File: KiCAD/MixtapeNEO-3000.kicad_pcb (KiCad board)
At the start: 2 copper layers, 99 x 64.8 mm, 62 parts, among them J1 CONN_01X04, J2 CONN_01X04, J4 Con_3-5V, J6 Sync_Jumper, SW1 SW_Push, SW2 SW_Push, SW3 SW_Push, U1 ATTINY85-20SU, U2 PAM8002

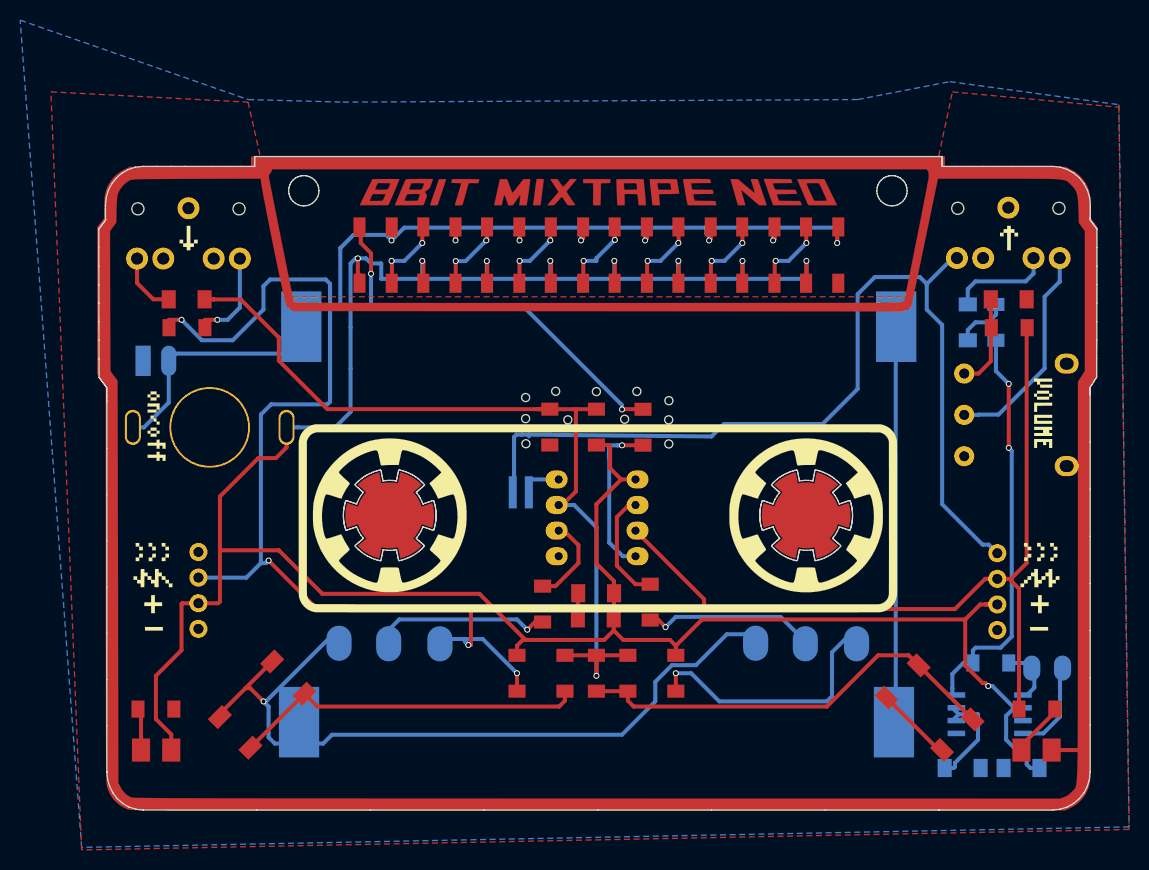
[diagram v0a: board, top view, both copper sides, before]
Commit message: reworked kicad 5 and many new design
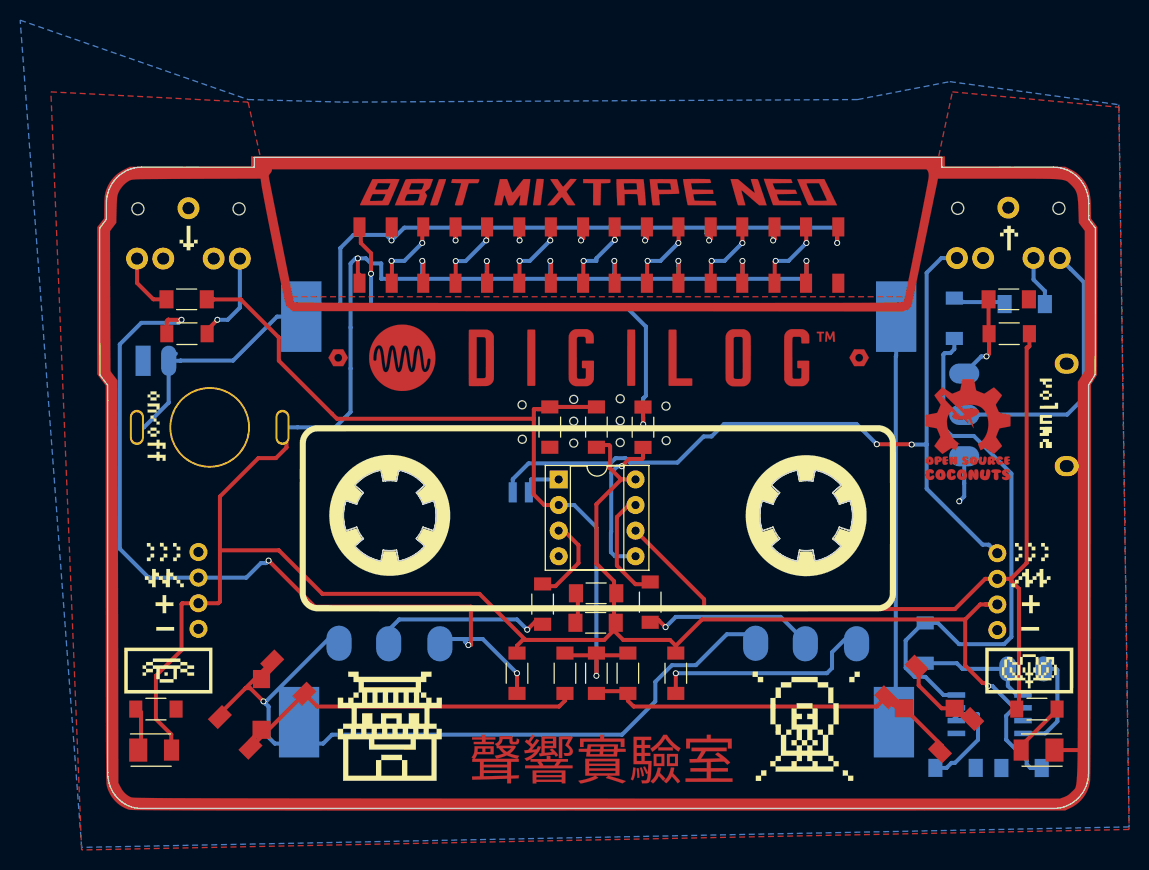
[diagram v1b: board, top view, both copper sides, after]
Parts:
- removed the ? at (142.9, 96.1)
- removed the ? at (147.0, 93.7)
- removed the ? at (142.8, 91.5)
- removed the ? at (145.8, 90.9)
- removed the ? at (149.9, 90.9)
- removed the ? at (142.8, 93.6)
- added ?: , 8BitMixtape3000-MutanMonkey:Speaker_Loch08, F.Cu at (142.5, 95.7)
- added ?: , 8BitMixtape3000-MutanMonkey:Speaker_Loch08, F.Cu at (142.5, 92.2)
- added ?: , 8BitMixtape3000-MutanMonkey:Speaker_Loch08, F.Cu at (147.6, 93.9)
- added ?: , 8BitMixtape3000-MutanMonkey:Speaker_Loch08, F.Cu at (147.6, 96.0)
- added ?: , 8BitMixtape3000-MutanMonkey:Speaker_Loch08, F.Cu at (147.6, 91.7)
- added Ref**: Val**, 8Bitmixtape_reworked:dusjagr, B.Cu at (149.9, 112.7)
- added Ref**: Val**, 8Bitmixtape_reworked:Coconut_logo_sm, F.Cu at (186.6, 94.7)
- added Ref**: Val**, 8Bitmixtape_reworked:CACR_chinese_hori, B.Cu at (150.4, 117.4)
- added Ref**: Val**, 8Bitmixtape_reworked:MadeInTaiwan_sm, B.Cu at (111.5, 101.7)
- C1, C2, C3, C4, C5, C6, C7: footprint 8Bitmixtape_reworked:C_1206_HandSoldering -> 8Bit_Eurorack:C_1206_3d
- D-OUT1, D-POW1: footprint 8Bitmixtape_reworked:LED_2835_minimal -> 8Bit_Eurorack:LED_PLCC_2835_Handsoldering
- J6: footprint 8Bitmixtape_reworked:Sync_jumper -> 8Bitmixtape_reworked:Sync_jumper_small
- NEO1, NEO2, NEO3, NEO4, NEO5, NEO6, NEO7, NEO8: footprint 8Bitmixtape_reworked:Mixtape_NEO_WS2812B -> 8Bit_Eurorack:Mixtape_NEO_WS2812B_3d
- R1, R10, R11, R12, R13, R14, R15, R2, R3, R4, R5, R6, R7, R8, R9, R99: footprint 8Bitmixtape_reworked:R_1206_HandSoldering -> 8Bit_Eurorack:R_1206_3d
- SW2, SW3: footprint 8Bitmixtape_reworked:TACTILE-PTH_6mm_SMD -> 8Bitmixtape_reworked:TACTILE-PTH_6mm_SMD_3d
- U1: footprint 8Bitmixtape_reworked:Attiny_DIP-8_W7.62mm_mod -> 8Bit_Eurorack:DIP-8_Attiny_with_Socket_3d
- board1: footprint 8Bitmixtape_reworked:Mixtape_reworked -> 8Bitmixtape_reworked:MixtapeNEO-3000_digilog
- moved R15 6.80 mm to (182.5, 115.9), turned to 90 degrees
- moved C5 5.93 mm to (192.3, 82.3), turned to 0 degrees
- moved ? 4.82 mm to (152.2, 96.0)
- moved R14 4.14 mm to (185.4, 83.7)
- moved Speaker1 2.13 mm to (191.2, 118.4)
- moved ? 2.08 mm to (156.8, 95.8)
- moved ? 1.80 mm to (152.2, 91.7)
- moved BT1 1.00 mm to (150.1, 83.6)
- moved C6 0.70 mm to (185.5, 128.3)
- moved ? 0.61 mm to (156.8, 92.4)
- moved R8 0.60 mm to (190.8, 85.2)
- moved R99 0.60 mm to (109.3, 85.2)
- moved ? 0.46 mm to (152.2, 93.8)
- moved C4 0.44 mm to (149.8, 113.9)
- turned SW3 to 135 degrees
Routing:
- net CV_IN: track 100.0 -> 84.5 mm
- net Net-(R14-Pad1): track 40.3 -> 55.7 mm, vias 2 -> 0
- net Sync_OUT: track 91.8 -> 81.1 mm, vias 0 -> 2
- net GND: track 169.0 -> 178.1 mm, vias 9 -> 10
- net Net-(NEO1-Pad2): track 39.2 -> 48.0 mm
- net Net-(R15-Pad1): track 5.72 -> 12.2 mm
- net Net-(Jack2-Pad2): track 21.5 -> 27.4 mm
- net Sound_OUT: track 10.2 -> 5.03 mm
- net Net-(BT1-Pad2): track 36.6 -> 41.0 mm
- net Net-(POT1-MAIN1-Pad1): track 26.1 -> 22.1 mm
- net But-R: track 43.2 -> 39.6 mm
- net +3V3: track 23.0 -> 25.6 mm
- net PB3: track 83.4 -> 85.7 mm
- net But-L: track 35.1 -> 37.4 mm
- net Net-(Speaker1-Pad2): track 8.78 -> 10.4 mm
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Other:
- board size 99 x 64.8 mm -> 98.8 x 64.6 mm
